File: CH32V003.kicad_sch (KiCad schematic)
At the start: 10 parts, among them J7 Program, SW1 SW_SPST, U5 CH32V003F4U6, X1 X322525MOB4SI

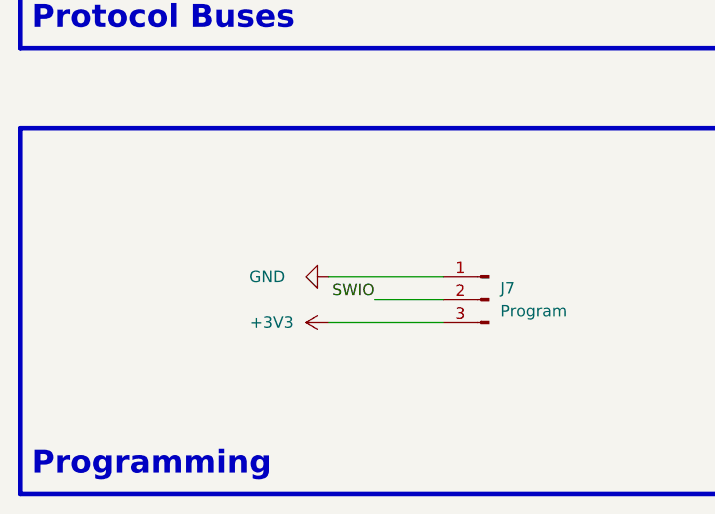
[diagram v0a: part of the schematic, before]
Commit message: BREAKING: updated CH32 programming pinout
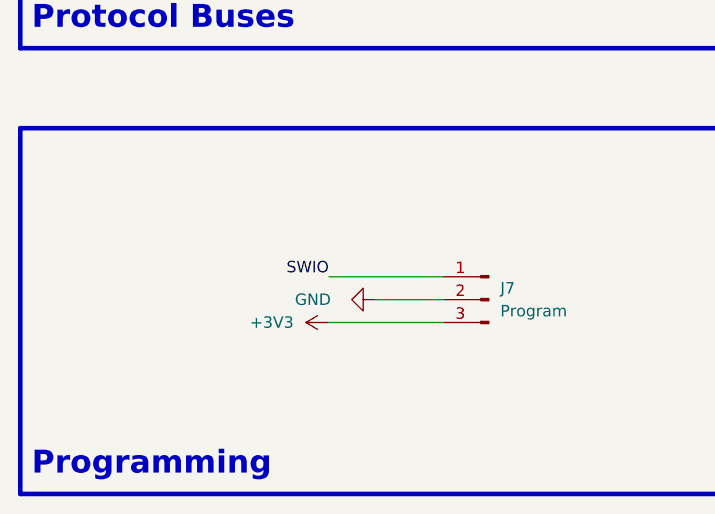
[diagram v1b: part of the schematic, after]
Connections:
- net GND: now also J7.2 (Pin_2); no longer J7.1 (Pin_1)
- net SWIO: now also J7.1 (Pin_1); no longer J7.2 (Pin_2)
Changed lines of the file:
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@@
 	(title_block
 		(title "MMS3_hat_HC-SR04-HX711")
-		(rev "A")
+		(date "2026-06-08")
+		(rev "1.1")
 		(company "MiniModucard System")
 		(comment 1 "Wojciech Szafrański")
@@
 	)
 	(label "SWIO"
-		(at 57.15 142.24 180)
+		(at 52.07 139.7 180)
 		(effects
 			(font
@@
 	(symbol
 		(lib_id "power:GND")
-		(at 52.07 139.7 270)
+		(at 57.15 142.24 270)
 		(unit 1)
 		(body_style 1)
@@
 		(dnp no)
 		(property "Reference" "#PWR054"
-			(at 45.72 139.7 0)
+			(at 50.8 142.24 0)
 			(hide yes)
 			(show_name no)
@@
 		)
 		(property "Value" "GND"
-			(at 45.212 139.7 90)
+			(at 50.292 142.24 90)
 			(show_name no)
 			(do_not_autoplace no)
@@
 		)
 		(property "Footprint" ""
-			(at 52.07 139.7 0)
+			(at 57.15 142.24 0)
 			(hide yes)
 			(show_name no)
@@
 		)
 		(property "Datasheet" ""
-			(at 52.07 139.7 0)
+			(at 57.15 142.24 0)
 			(hide yes)
 			(show_name no)
@@
 		)
 		(property "Description" "Power symbol creates a global label with name \"GND\" , ground"
-			(at 52.07 139.7 0)
-			(hide yes)
-			(show_name no)
+			(at 57.15 142.24 0)
+			(hide yes)
+			(show_name no)
